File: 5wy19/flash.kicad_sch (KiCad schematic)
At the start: 1 part, among them IC2 AM29F400BB-90SC

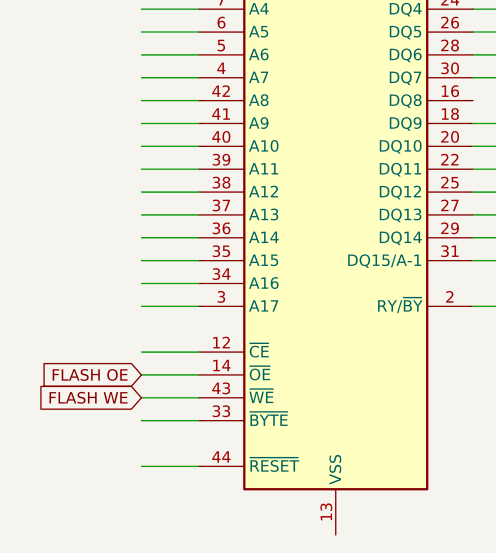
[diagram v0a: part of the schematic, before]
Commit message: Mapped out more pins of MCU and relevant circuits
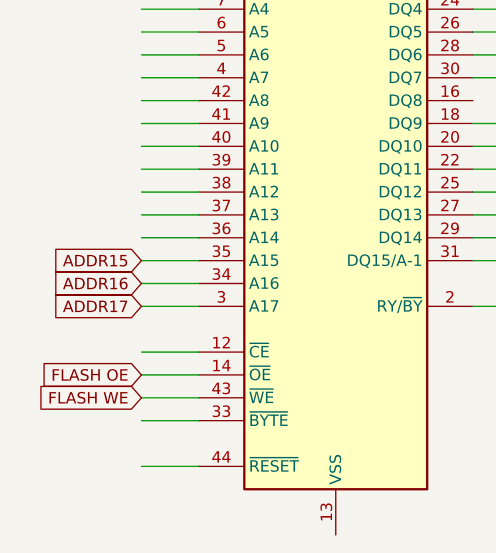
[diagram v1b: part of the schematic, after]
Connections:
- net ADDR17: now reaches IC2.3 (A17)
- net ADDR16: now reaches IC2.34 (A16)
- net ADDR15: now reaches IC2.35 (A15)
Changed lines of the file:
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@@
+		)
+	)
+	(global_label "ADDR16"
+		(shape input)
+		(at 123.19 109.22 180)
+		(fields_autoplaced yes)
+		(effects
+			(font
+				(size 1.27 1.27)
+			)
+			(justify right)
+		)
+		(property "Intersheetrefs" "${INTERSHEET_REFS}"
+			(at 112.8872 109.22 0)
+			(effects
+				(font
+					(size 1.27 1.27)
+				)
+				(justify right)
+				(hide yes)
+			)
 		)
 	)
@@
 			(effects
 				(font
+					(size 1.27 1.27)
+				)
+				(justify right)
+				(hide yes)
+			)
+		)
+	)
+	(global_label "ADDR15"
+		(shape input)
+		(at 123.19 106.68 180)
+		(fields_autoplaced yes)
+		(effects
+			(font
+				(size 1.27 1.27)
+			)
+			(justify right)
+		)
+		(property "Intersheetrefs" "${INTERSHEET_REFS}"
+			(at 112.8872 106.68 0)
+			(effects
+				(font
+					(size 1.27 1.27)
+				)
+				(justify right)
+				(hide yes)
+			)
+		)
+	)
+	(global_label "ADDR17"
+		(shape input)
+		(at 123.19 111.76 180)
+		(fields_autoplaced yes)
+		(effects
+			(font
+				(size 1.27 1.27)
+			)
+			(justify right)
+		)
+		(property "Intersheetrefs" "${INTERSHEET_REFS}"
+			(at 112.8872 111.76 0)
+			(effects
+				(font

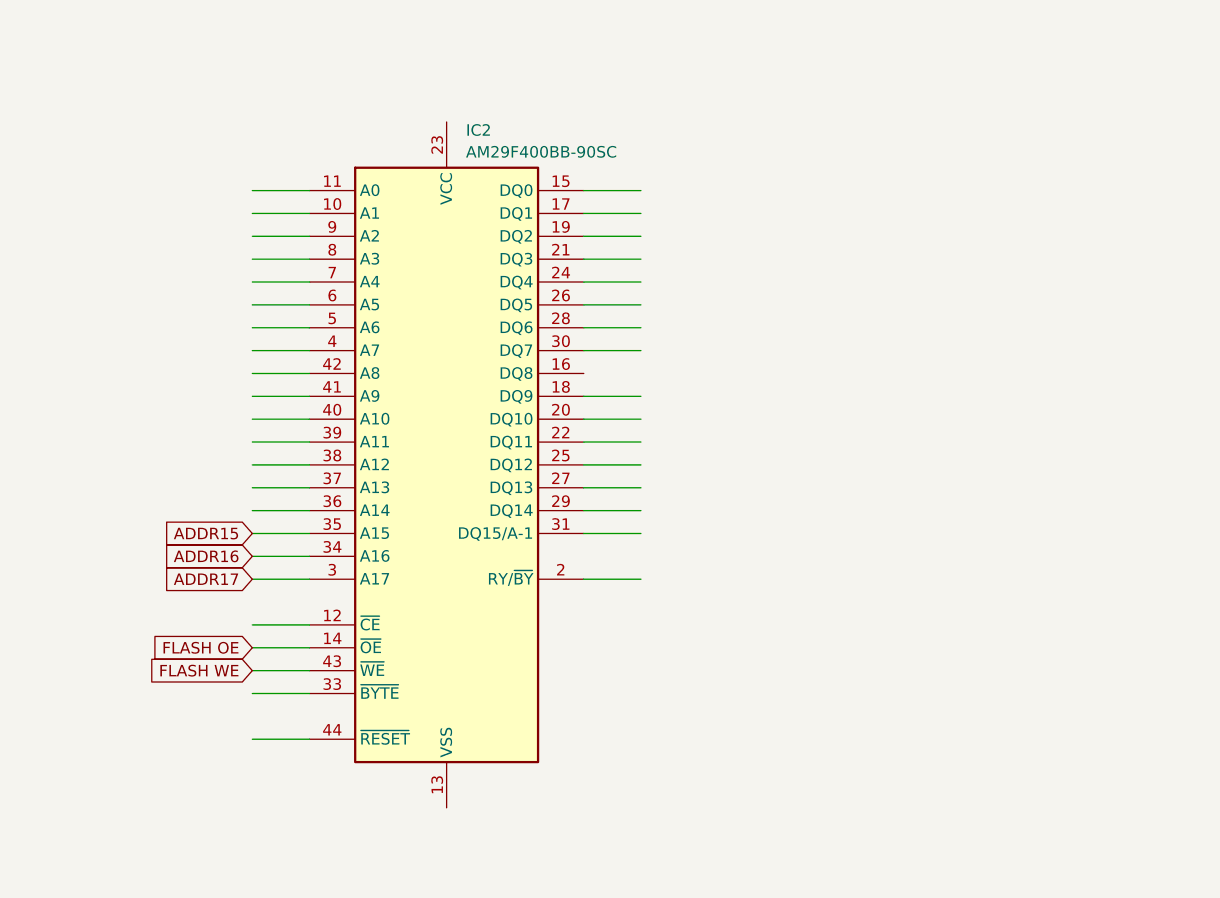
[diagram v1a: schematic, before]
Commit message: Finished most of the subsystems
-- MCU finished
-- Flash finished
-- Power Supply finished
-- I/O Drivers finished
-- CANBUS finished
-- Knock Control finished
-- Connector finished
-- Ignition Driver finished
-- Sensor Logic mostly finished
-- Logic ICs need some work
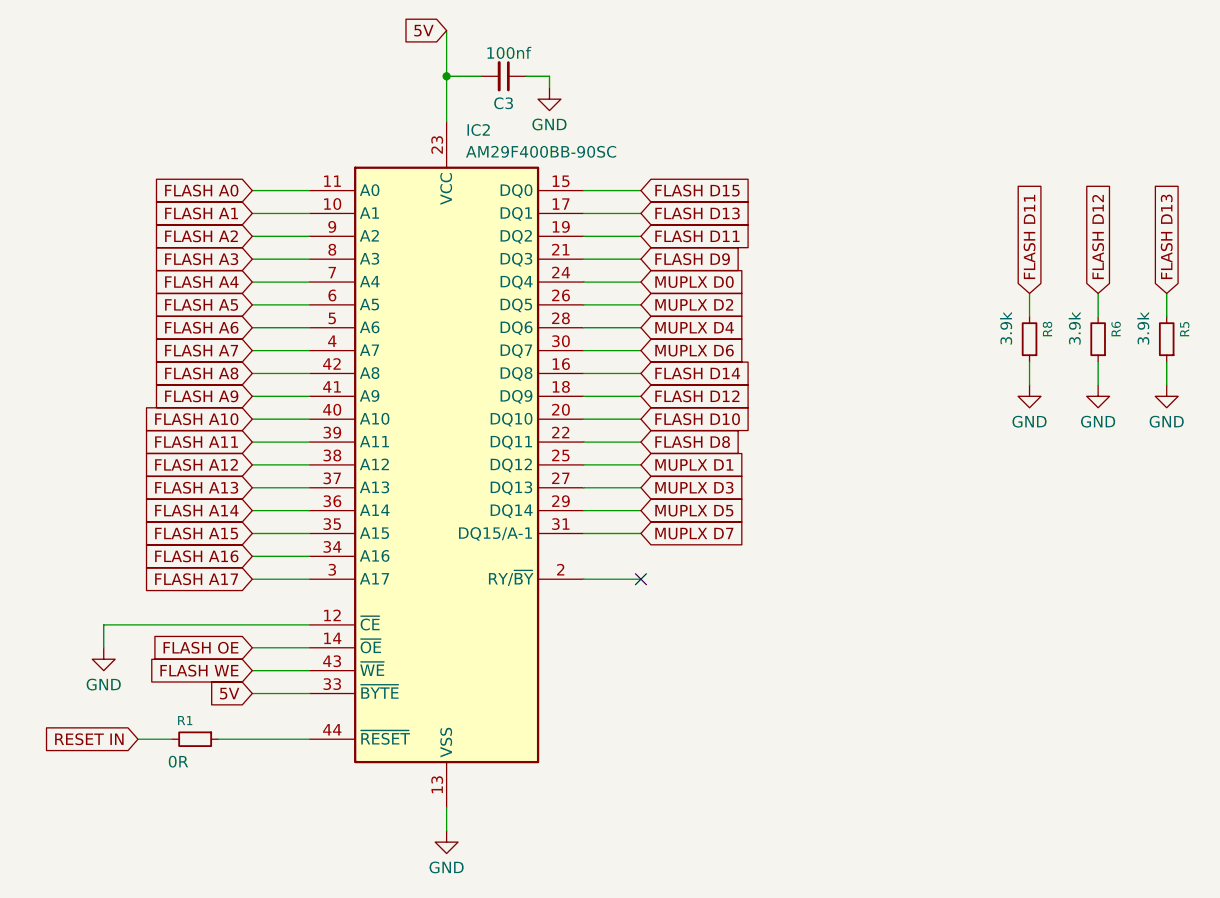
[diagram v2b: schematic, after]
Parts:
- added C3: 100nf, symbol Device:C_Small
- added R1: 0R, symbol Device:R_Small
- added R5, R6, R8: 3.9k, symbol Device:R_Small
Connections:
- net FLASH A1: now reaches IC2.10 (A1)
- net FLASH A0: now reaches IC2.11 (A0)
- net GND: now reaches IC2.12 (~{CE})
- net GND: now also IC2.13 (VSS), IC2.32 (VSS), C3.1, R5.1, R6.1, R8.1
- net FLASH D15: now reaches IC2.15 (DQ0)
- net FLASH D14: now reaches IC2.16 (DQ8)
- net FLASH D13: now reaches IC2.17 (DQ1)
- net FLASH D13: now also R5.2
- net FLASH D12: now reaches IC2.18 (DQ9)
- net FLASH D12: now also R6.2
- net FLASH D11: now reaches IC2.19 (DQ2)
- net FLASH D11: now also R8.2
- net FLASH D10: now reaches IC2.20 (DQ10)
- net FLASH D9: now reaches IC2.21 (DQ3)
- net FLASH D8: now reaches IC2.22 (DQ11)
- net 5V: now reaches IC2.23 (VCC)
- net 5V: now also IC2.33 (~{BYTE}), C3.2
- net MUPLX D0: now reaches IC2.24 (DQ4)
- net MUPLX D1: now reaches IC2.25 (DQ12)
- net MUPLX D2: now reaches IC2.26 (DQ5)
- net MUPLX D3: now reaches IC2.27 (DQ13)
- net MUPLX D4: now reaches IC2.28 (DQ6)
- net MUPLX D5: now reaches IC2.29 (DQ14)
- net MUPLX D6: now reaches IC2.30 (DQ7)
- net MUPLX D7: now reaches IC2.31 (DQ15/A-1)
- net FLASH A14: now reaches IC2.36 (A14)
- net FLASH A13: now reaches IC2.37 (A13)
- net FLASH A12: now reaches IC2.38 (A12)
- net FLASH A11: now reaches IC2.39 (A11)
- net FLASH A7: now reaches IC2.4 (A7)
- net FLASH A10: now reaches IC2.40 (A10)
- net FLASH A9: now reaches IC2.41 (A9)
- net FLASH A8: now reaches IC2.42 (A8)
- net at IC2.44 (~{RESET}): now also R1.1
- net FLASH A6: now reaches IC2.5 (A6)
- net FLASH A5: now reaches IC2.6 (A5)
- net FLASH A4: now reaches IC2.7 (A4)
- net FLASH A3: now reaches IC2.8 (A3)
- net FLASH A2: now reaches IC2.9 (A2)
- net ADDR15 renamed FLASH A15
- net ADDR16 renamed FLASH A16
- net ADDR17 renamed FLASH A17
- new net RESET IN: R1.2
- no-connect marks 0 -> 1
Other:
- title: (none) -> SMIK43 5WY19 Rev. Eng

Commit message: Final schematic (except maybe some oversights)
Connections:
- net 5V: now also C3.1; no longer C3.2
- net FLASH D11: now also R8.1; no longer R8.2
- net FLASH D12: now also R6.1; no longer R6.2
- net FLASH D13: now also R5.1; no longer R5.2
- net GND: now also C3.2, R5.2, R6.2, R8.2; no longer C3.1, R5.1, R6.1, R8.1
- net MUPLX D0 renamed MLTPLX D0
- net MUPLX D1 renamed MLTPLX D1
- net MUPLX D2 renamed MLTPLX D2
- net MUPLX D3 renamed MLTPLX D3
- net MUPLX D4 renamed MLTPLX D4
- net MUPLX D5 renamed MLTPLX D5
- net MUPLX D6 renamed MLTPLX D6
- net MUPLX D7 renamed MLTPLX D7
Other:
- moved on the sheet: C3, R5, R6, R8
